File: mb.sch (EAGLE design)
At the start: 6 parts, among them J1 PJ-002BH-SMT-TR, U1 PEM1-S12-S5-S

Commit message: Adding io components, level shifters
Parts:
- added J2, J3, J4, J5: MOLEX_70543-0003MOLEX_70543-0003_0_0, Molex - 70543-0003:MOLEX_70543-0003MOLEX_70543-0003_0_0
- added JP1, JP2, JP3, JP4: (no value), pinhead:PINHD-1X3/90
- added Q1, Q2, Q3, Q4: TN0702N3-G, SamacSys_Parts:TN0702N3-G
- added R1, R2, R3, R4, R5, R6, R7, R8: 10k, ref_lib:YAGEO-CFR-25
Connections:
- new net +3.3V: JP1.3, JP2.3, JP3.3, JP4.3, Q1.G, Q2.G, Q3.G, Q4.G, R1.2, R3.2, R5.2, R7.2
- new net BOOL1: JP1.2
- new net BOOL2: JP2.2
- new net BOOL3: JP3.2
- new net BOOL4: JP4.2
- new net LC1: Q4.S, R7.1
- new net LC2: Q3.S, R5.1
- new net LC3: Q2.S, R3.1
- new net LC4: Q1.S, R1.1
- new net LED1: J2.2, Q4.D, R8.1
- new net LED2: J3.2, Q3.D, R6.1
- new net LED3: J4.2, Q2.D, R4.1
- new net LED4: J5.2, Q1.D, R2.1
- net +12V: now also J2.4, J3.4, J4.4, J5.4
- net +5V: now also R2.2, R4.2, R6.2, R8.2
- net GND: now also J2.1, J2.3, J3.1, J3.3, J4.1, J4.3, J5.1, J5.3, JP1.1, JP2.1, JP3.1, JP4.1

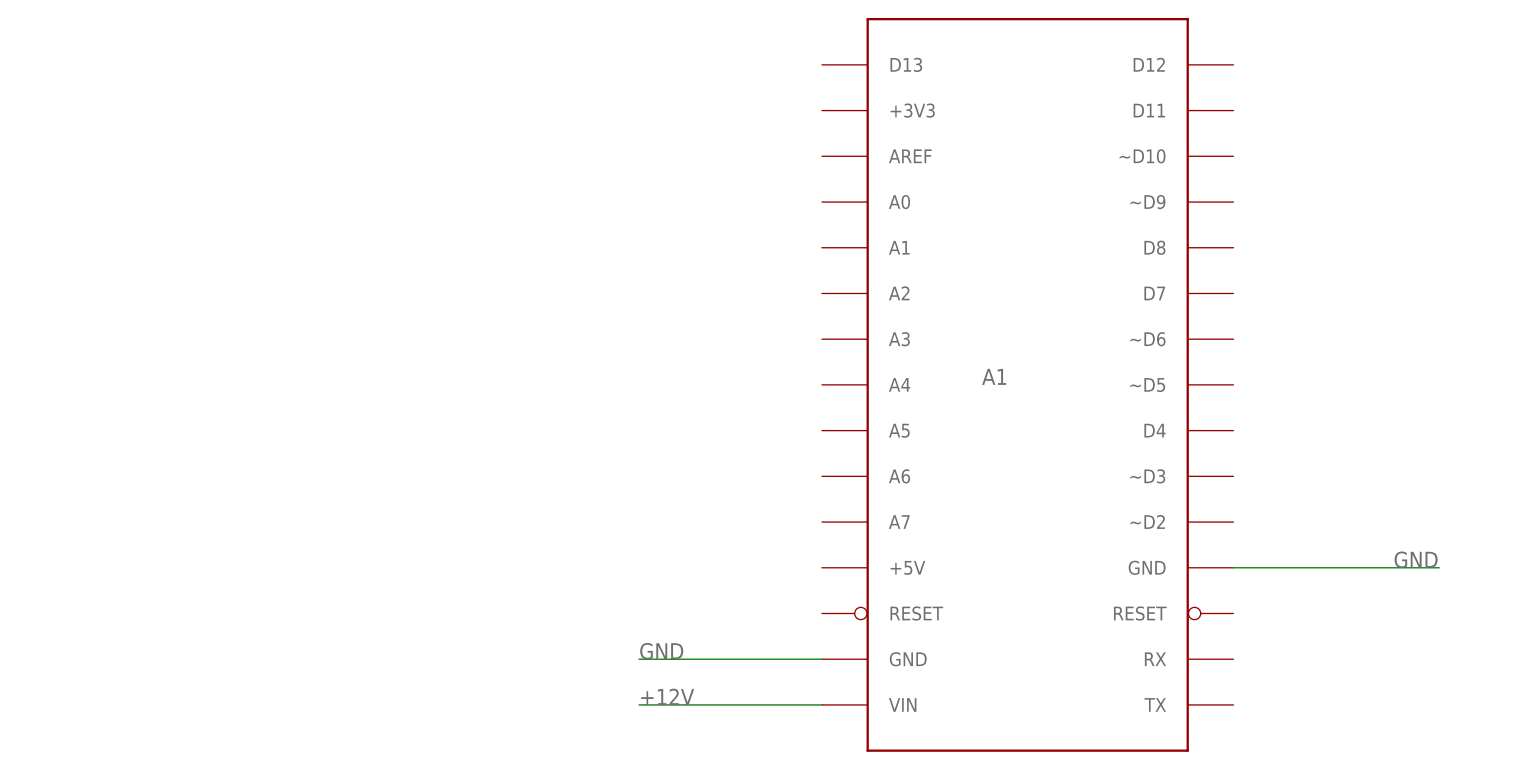
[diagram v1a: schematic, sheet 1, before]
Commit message: Final Board layout with eeprom
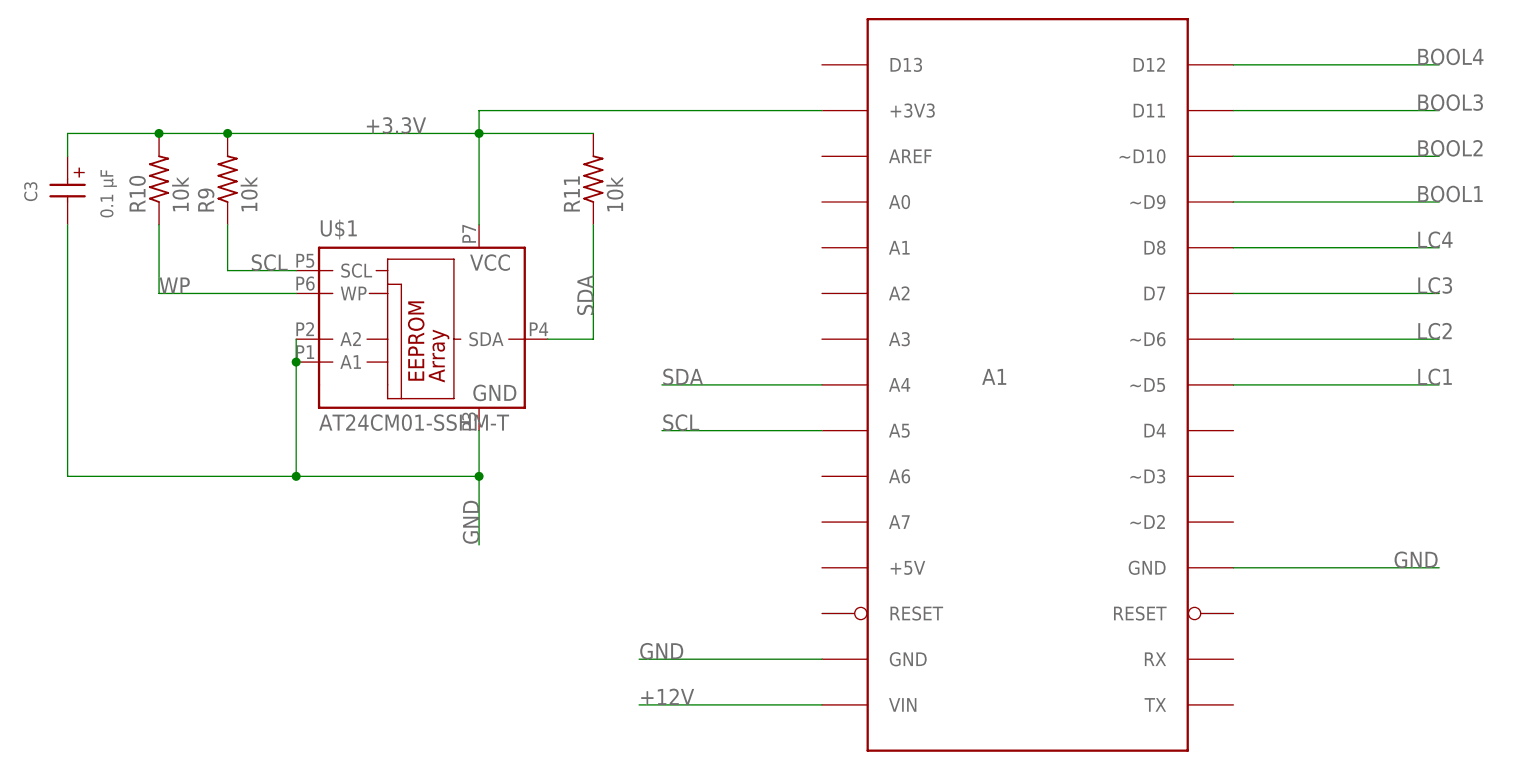
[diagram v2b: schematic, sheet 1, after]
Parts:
- added C3: 0.1 µF, 860020672008_Eagle_WCAP-ATG5_rev20a:WCAP-ATG5_5X11_860020672001
- added R10, R11, R9: 10k, ref_lib:YAGEO-CFR-25
- added U$1: AT24CM01-SSHM-T, ref_lib:AT24CM01-SSHM-T
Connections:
- new net SCL: A1.A5, R9.1, U$1.SCL
- new net SDA: A1.A4, R11.1, U$1.SDA
- new net WP: R10.1, U$1.WP
- net +3.3V: now also A1.+3V3, C3.+, R10.2, R11.2, R9.2, U$1.VCC
- net BOOL1: now also A1.~D9
- net BOOL2: now also A1.~D10
- net BOOL3: now also A1.D11
- net BOOL4: now also A1.D12
- net GND: now also C3.-, U$1.A1, U$1.A2, U$1.GND
- net LC1: now also A1.~D5
- net LC2: now also A1.~D6
- net LC3: now also A1.D7
- net LC4: now also A1.D8
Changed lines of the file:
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@@
 <part name="JP3" library="pinhead" library_urn="urn:adsk.eagle:library:325" deviceset="PINHD-1X3" device="/90" package3d_urn="urn:adsk.eagle:package:22459/2"/>
 <part name="JP4" library="pinhead" library_urn="urn:adsk.eagle:library:325" deviceset="PINHD-1X3" device="/90" package3d_urn="urn:adsk.eagle:package:22459/2"/>
+<part name="U$1" library="ref_lib" deviceset="AT24CM01-SSHM-T" device=""/>
+<part name="R9" library="ref_lib" deviceset="YAGEO-CFR-25" device="" value="10k"/>
+<part name="R10" library="ref_lib" deviceset="YAGEO-CFR-25" device="" value="10k"/>
+<part name="R11" library="ref_lib" deviceset="YAGEO-CFR-25" device="" value="10k"/>
+<part name="C3" library="860020672008_Eagle_WCAP-ATG5_rev20a" deviceset="WCAP-ATG5_5X11" device="" package3d_urn="urn:adsk.eagle:package:18308011/2" technology="_860020672001" value="0.1  µF "/>
 </parts>
 <sheets>
@@
 <instance part="A1" gate="G$1" x="78.74" y="48.26" smashed="yes">
 <attribute name="NAME" x="73.66" y="48.26" size="1.778" layer="95"/>
+</instance>
+<instance part="U$1" gate="G$1" x="10.16" y="53.34" smashed="yes">
+<attribute name="NAME" x="0" y="64.77" size="1.778" layer="95"/>
+<attribute name="VALUE" x="0" y="43.18" size="1.778" layer="96"/>
+</instance>
+<instance part="R9" gate="G$1" x="-10.16" y="71.12" smashed="yes" rot="R90">
+<attribute name="NAME" x="-11.6586" y="67.31" size="1.778" layer="95" rot="R90"/>
+<attribute name="VALUE" x="-6.858" y="67.31" size="1.778" layer="96" rot="R90"/>
+</instance>
+<instance part="R10" gate="G$1" x="-17.78" y="71.12" smashed="yes" rot="R90">
+<attribute name="NAME" x="-19.2786" y="67.31" size="1.778" layer="95" rot="R90"/>
+<attribute name="VALUE" x="-14.478" y="67.31" size="1.778" layer="96" rot="R90"/>
+</instance>
+<instance part="R11" gate="G$1" x="30.48" y="71.12" smashed="yes" rot="R90">
+<attribute name="NAME" x="28.9814" y="67.31" size="1.778" layer="95" rot="R90"/>
+<attribute name="VALUE" x="33.782" y="67.31" size="1.778" layer="96" rot="R90"/>
+</instance>
+<instance part="C3" gate="G$1" x="-27.94" y="68.58" smashed="yes" rot="R90">
+<attribute name="NAME" x="-31.32" y="69.755" size="1.4224" layer="95" rot="R90" align="bottom-center"/>
+<attribute name="VALUE" x="-22.865" y="69.495" size="1.4224" layer="96" rot="R90" align="bottom-center"/>
 </instance>
 </instances>
@@
 <label x="119.38" y="27.94" size="1.778" layer="95"/>
 </segment>
+<segment>
+<pinref part="U$1" gate="G$1" pin="A1"/>
+<wire x1="-2.54" y1="50.8" x2="-2.54" y2="38.1" width="0.1524" layer="91"/>
+<wire x1="-2.54" y1="38.1" x2="17.78" y2="38.1" width="0.1524" layer="91"/>
+<pinref part="U$1" gate="G$1" pin="GND"/>
+<wire x1="17.78" y1="38.1" x2="17.78" y2="43.18" width="0.1524" layer="91"/>
+<wire x1="17.78" y1="38.1" x2="17.78" y2="30.48" width="0.1524" layer="91"/>
+<junction x="17.78" y="38.1"/>
+<pinref part="U$1" gate="G$1" pin="A2"/>
+<wire x1="-2.54" y1="53.34" x2="-2.54" y2="50.8" width="0.1524" layer="91"/>
+<junction x="-2.54" y="50.8"/>
+<label x="17.78" y="30.48" size="1.778" layer="95" rot="R90"/>
+<pinref part="C3" gate="G$1" pin="-"/>
+<wire x1="-27.94" y1="66.04" x2="-27.94" y2="38.1" width="0.1524" layer="91"/>
+<wire x1="-27.94" y1="38.1" x2="-2.54" y2="38.1" width="0.1524" layer="91"/>
+<junction x="-2.54" y="38.1"/>
+</segment>
 </net>
+<net name="LC1" class="0">
+<segment>
+<pinref part="A1" gate="G$1" pin="~D5"/>
+<wire x1="101.6" y1="48.26" x2="124.46" y2="48.26" width="0.1524" layer="91"/>
+<label x="121.92" y="48.26" size="1.778" layer="95"/>
+</segment>
+</net>
+<net name="LC2" class="0">
+<segment>
+<pinref part="A1" gate="G$1" pin="~D6"/>
+<wire x1="101.6" y1="53.34" x2="124.46" y2="53.34" width="0.1524" layer="91"/>
+<label x="121.92" y="53.34" size="1.778" layer="95"/>
+</segment>
+</net>
+<net name="LC3" class="0">
+<segment>
+<pinref part="A1" gate="G$1" pin="D7"/>
+<wire x1="101.6" y1="58.42" x2="124.46" y2="58.42" width="0.1524" layer="91"/>
+<label x="121.92" y="58.42" size="1.778" layer="95"/>
+</segment>
+</net>
+<net name="LC4" class="0">
+<segment>
+<pinref part="A1" gate="G$1" pin="D8"/>
+<wire x1="101.6" y1="63.5" x2="124.46" y2="63.5" width="0.1524" layer="91"/>
+<label x="121.92" y="63.5" size="1.778" layer="95"/>
+</segment>
+</net>
+<net name="BOOL4" class="0">
+<segment>
+<pinref part="A1" gate="G$1" pin="D12"/>
+<wire x1="101.6" y1="83.82" x2="124.46" y2="83.82" width="0.1524" layer="91"/>
+<label x="121.92" y="83.82" size="1.778" layer="95"/>
+</segment>
+</net>
+<net name="BOOL3" class="0">
+<segment>
+<pinref part="A1" gate="G$1" pin="D11"/>
+<wire x1="101.6" y1="78.74" x2="124.46" y2="78.74" width="0.1524" layer="91"/>
+<label x="121.92" y="78.74" size="1.778" layer="95"/>
+</segment>
+</net>
+<net name="BOOL2" class="0">
+<segment>
+<pinref part="A1" gate="G$1" pin="~D10"/>
+<wire x1="101.6" y1="73.66" x2="124.46" y2="73.66" width="0.1524" layer="91"/>
+<label x="121.92" y="73.66" size="1.778" layer="95"/>
+</segment>
+</net>
+<net name="BOOL1" class="0">
+<segment>
+<pinref part="A1" gate="G$1" pin="~D9"/>
+<wire x1="101.6" y1="68.58" x2="124.46" y2="68.58" width="0.1524" layer="91"/>
+<label x="121.92" y="68.58" size="1.778" layer="95"/>
+</segment>
+</net>
+<net name="WP" class="0">
+<segment>
+<pinref part="R10" gate="G$1" pin="1"/>
+<pinref part="U$1" gate="G$1" pin="WP"/>
+<wire x1="-17.78" y1="66.04" x2="-17.78" y2="58.42" width="0.1524" layer="91"/>
+<wire x1="-17.78" y1="58.42" x2="-2.54" y2="58.42" width="0.1524" layer="91"/>
+<label x="-17.78" y="58.42" size="1.778" layer="95"/>
+</segment>
+</net>
+<net name="SCL" class="0">
+<segment>
+<pinref part="R9" gate="G$1" pin="1"/>
+<pinref part="U$1" gate="G$1" pin="SCL"/>
+<wire x1="-10.16" y1="66.04" x2="-10.16" y2="60.96" width="0.1524" layer="91"/>
+<wire x1="-10.16" y1="60.96" x2="-2.54" y2="60.96" width="0.1524" layer="91"/>
+<label x="-7.62" y="60.96" size="1.778" layer="95"/>
+</segment>
+<segment>
+<pinref part="A1" gate="G$1" pin="A5"/>
+<wire x1="55.88" y1="43.18" x2="38.1" y2="43.18" width="0.1524" layer="91"/>
+<label x="38.1" y="43.18" size="1.778" layer="95"/>
+</segment>
+</net>
+<net name="SDA" class="0">
+<segment>
+<pinref part="R11" gate="G$1" pin="1"/>
+<pinref part="U$1" gate="G$1" pin="SDA"/>
+<wire x1="30.48" y1="66.04" x2="30.48" y2="53.34" width="0.1524" layer="91"/>
+<wire x1="30.48" y1="53.34" x2="25.4" y2="53.34" width="0.1524" layer="91"/>
+<label x="30.48" y="55.88" size="1.778" layer="95" rot="R90"/>
+</segment>
+<segment>
+<pinref part="A1" gate="G$1" pin="A4"/>
+<wire x1="55.88" y1="48.26" x2="38.1" y2="48.26" width="0.1524" layer="91"/>
+<label x="38.1" y="48.26" size="1.778" layer="95"/>
+</segment>
+</net>
+<net name="+3.3V" class="0">
+<segment>
+<pinref part="U$1" gate="G$1" pin="VCC"/>
+<wire x1="17.78" y1="66.04" x2="17.78" y2="76.2" width="0.1524" layer="91"/>
+<pinref part="R11" gate="G$1" pin="2"/>
+<wire x1="17.78" y1="76.2" x2="17.78" y2="78.74" width="0.1524" layer="91"/>
+<wire x1="30.48" y1="76.2" x2="17.78" y2="76.2" width="0.1524" layer="91"/>
+<junction x="17.78" y="76.2"/>
+<pinref part="R9" gate="G$1" pin="2"/>
+<wire x1="-10.16" y1="76.2" x2="17.78" y2="76.2" width="0.1524" layer="91"/>
+<pinref part="R10" gate="G$1" pin="2"/>
+<wire x1="-17.78" y1="76.2" x2="-10.16" y2="76.2" width="0.1524" layer="91"/>
+<junction x="-10.16" y="76.2"/>
+<pinref part="C3" gate="G$1" pin="+"/>
+<wire x1="-27.94" y1="73.66" x2="-27.94" y2="76.2" width="0.1524" layer="91"/>
+<wire x1="-27.94" y1="76.2" x2="-17.78" y2="76.2" width="0.1524" layer="91"/>
+<junction x="-17.78" y="76.2"/>
+<label x="5.08" y="76.2" size="1.778" layer="95"/>
+<pinref part="A1" gate="G$1" pin="+3V3"/>
+<wire x1="55.88" y1="78.74" x2="17.78" y2="78.74" width="0.1524" layer="91"/>
+</segment>
+</net>

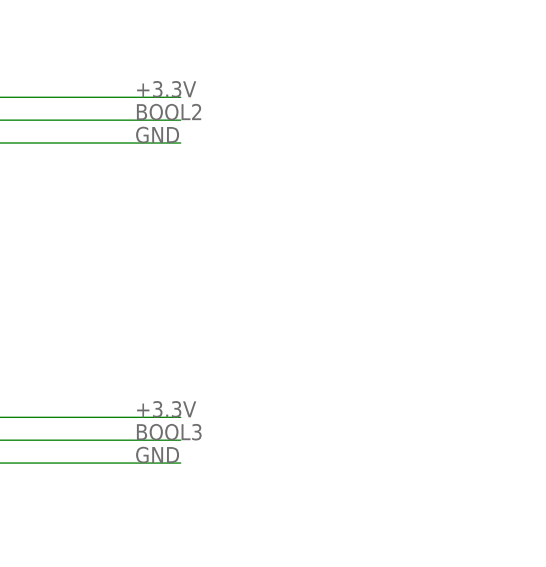
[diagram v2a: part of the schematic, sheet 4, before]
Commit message: Finish 1st layout. Add cam profile
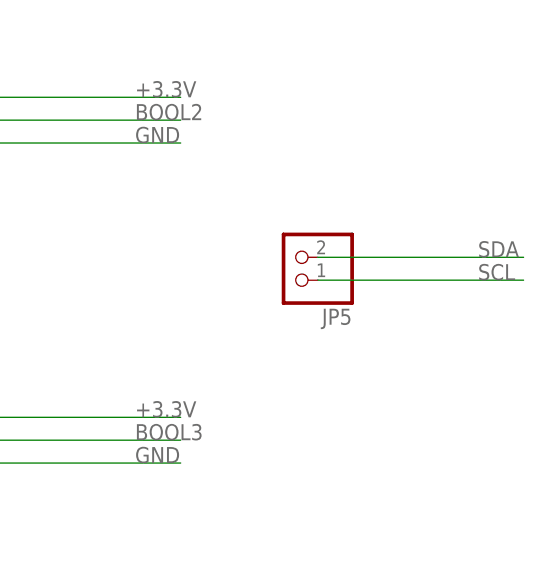
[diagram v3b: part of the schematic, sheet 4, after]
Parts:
- added JP5: (no value), pinhead:PINHD-1X2
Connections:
- net SCL: now also JP5.1
- net SDA: now also JP5.2
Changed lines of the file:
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@@
 <part name="R11" library="ref_lib" deviceset="YAGEO-CFR-25" device="" value="10k"/>
 <part name="C3" library="860020672008_Eagle_WCAP-ATG5_rev20a" deviceset="WCAP-ATG5_5X11" device="" package3d_urn="urn:adsk.eagle:package:18308011/2" technology="_860020672001" value="0.1  µF "/>
+<part name="JP5" library="pinhead" library_urn="urn:adsk.eagle:library:325" deviceset="PINHD-1X2" device="" package3d_urn="urn:adsk.eagle:package:22435/2"/>
 </parts>
 <sheets>
@@
 <attribute name="VALUE" x="90.17" y="22.86" size="1.778" layer="96" rot="R180"/>
 </instance>
+<instance part="JP5" gate="G$1" x="142.24" y="73.66" smashed="yes" rot="R180">
+<attribute name="NAME" x="148.59" y="67.945" size="1.778" layer="95" rot="R180"/>
+<attribute name="VALUE" x="148.59" y="78.74" size="1.778" layer="96" rot="R180"/>
+</instance>
 </instances>
 <busses>
@@
 </segment>
 </net>
+<net name="SDA" class="0">
+<segment>
+<pinref part="JP5" gate="G$1" pin="2"/>
+<wire x1="144.78" y1="73.66" x2="167.64" y2="73.66" width="0.1524" layer="91"/>
+<label x="162.56" y="73.66" size="1.778" layer="95"/>
+</segment>
+</net>
+<net name="SCL" class="0">
+<segment>
+<pinref part="JP5" gate="G$1" pin="1"/>
+<wire x1="144.78" y1="71.12" x2="167.64" y2="71.12" width="0.1524" layer="91"/>
+<label x="162.56" y="71.12" size="1.778" layer="95"/>
+</segment>
+</net>
